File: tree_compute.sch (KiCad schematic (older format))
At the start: 15 parts, among them J1 AVR-ISP-6, J10 Conn_01x01, J11 Conn_01x01, J2 Conn_01x01, J3 Conn_01x01, J6 Conn_01x01, J7 Conn_01x01, J8 Conn_01x01, J9 Conn_01x01, U1 ATtiny13A-SSU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

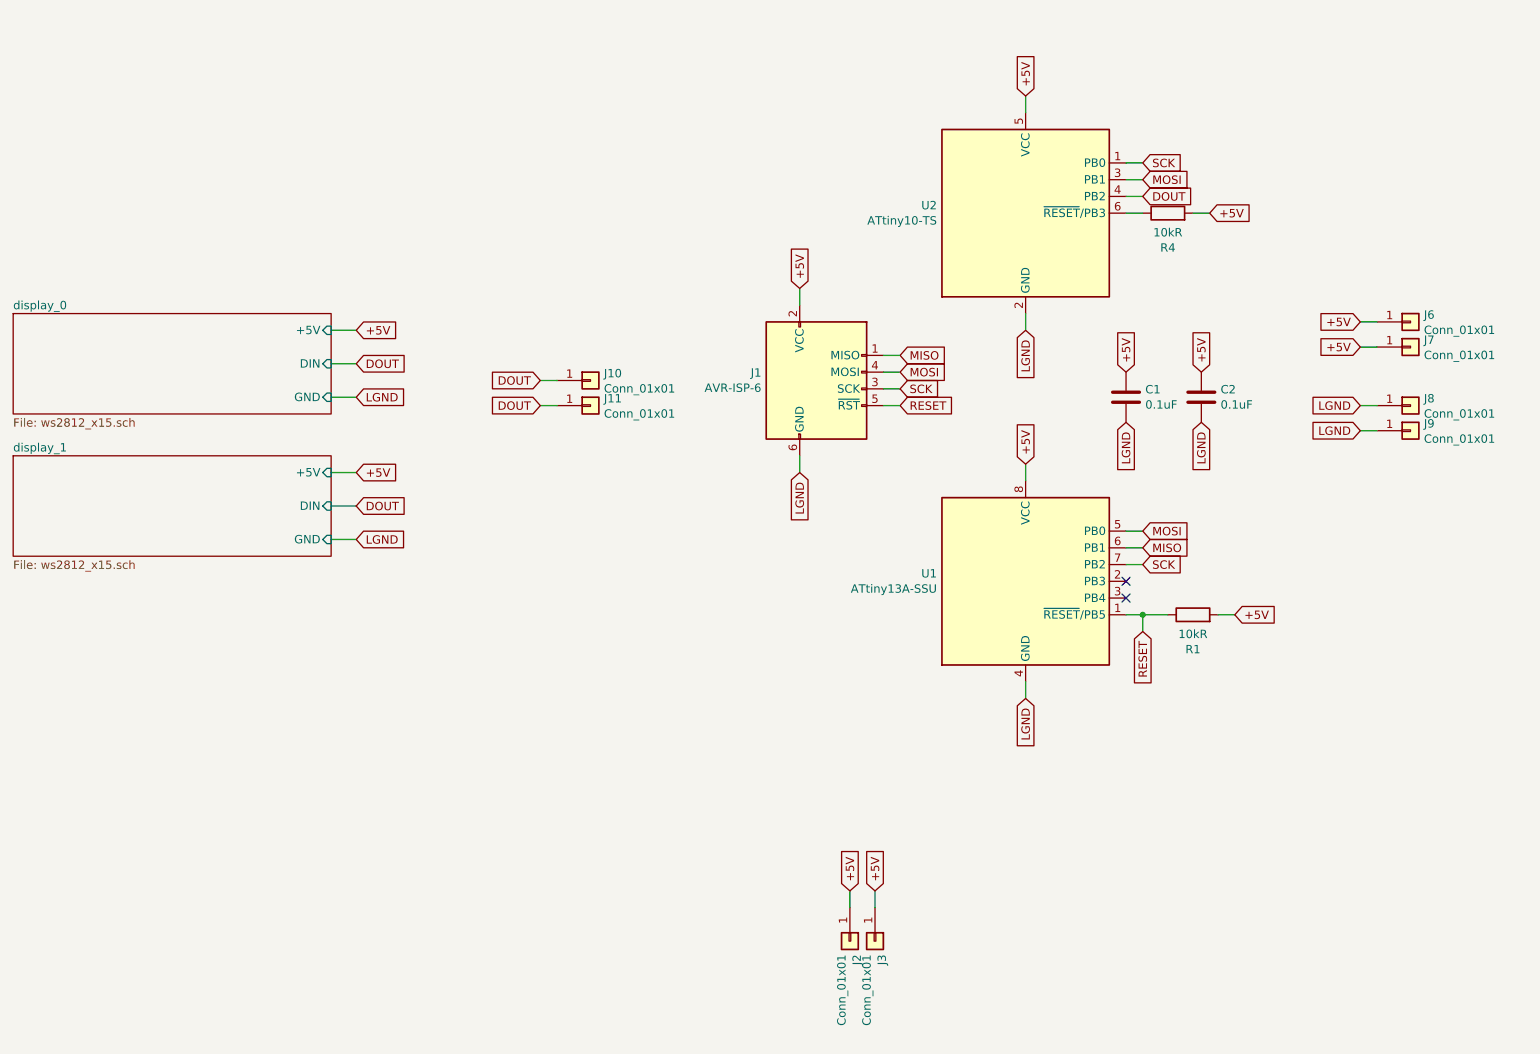
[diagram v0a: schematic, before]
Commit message: Update with changes to use attiny13a only
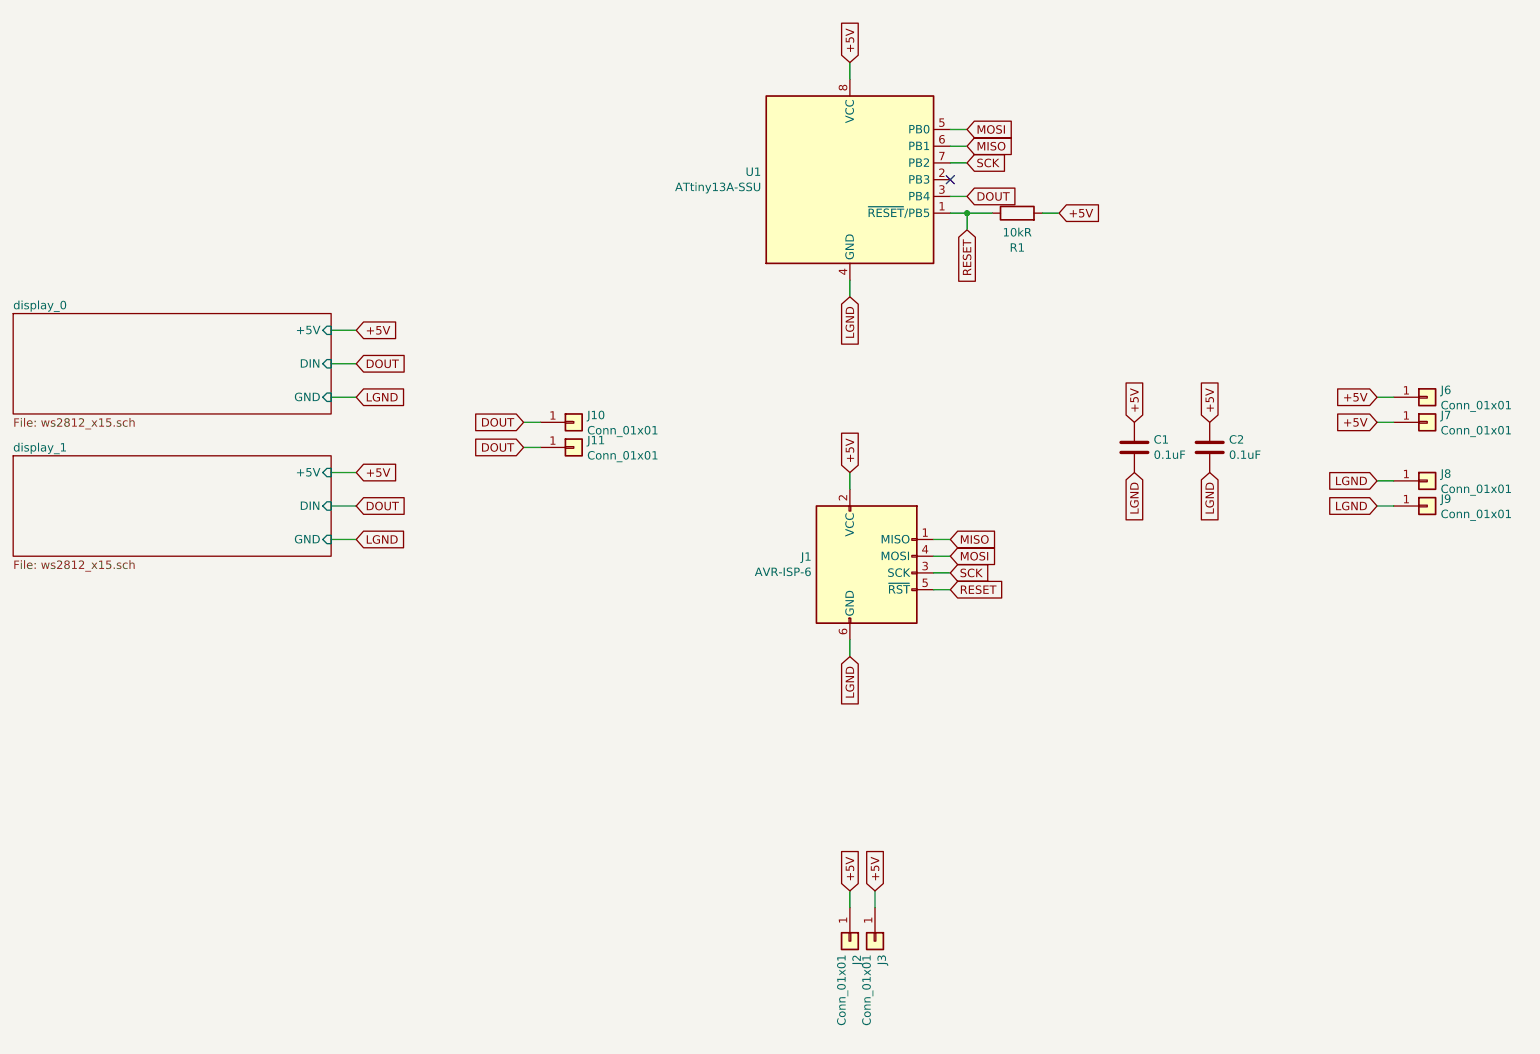
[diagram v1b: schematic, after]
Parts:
- removed R4: 10kR, Resistor_SMD:R_0805_2012Metric, symbol Device:R
- removed U2: ATtiny10-TS, Package_TO_SOT_SMD:SOT-23-6, symbol MCU_Microchip_ATtiny:ATtiny10-TS
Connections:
- net DOUT: now also U1.3 (PB4)
- no-connect marks 2 -> 1
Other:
- moved on the sheet: C1, C2, J1, J10, J11, J6, J7, J8, J9, R1, U1
